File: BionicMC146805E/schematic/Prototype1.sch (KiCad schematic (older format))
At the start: 10 parts, among them SW1 TSD1265, U1 MC146805E2P, U2 74HCT541

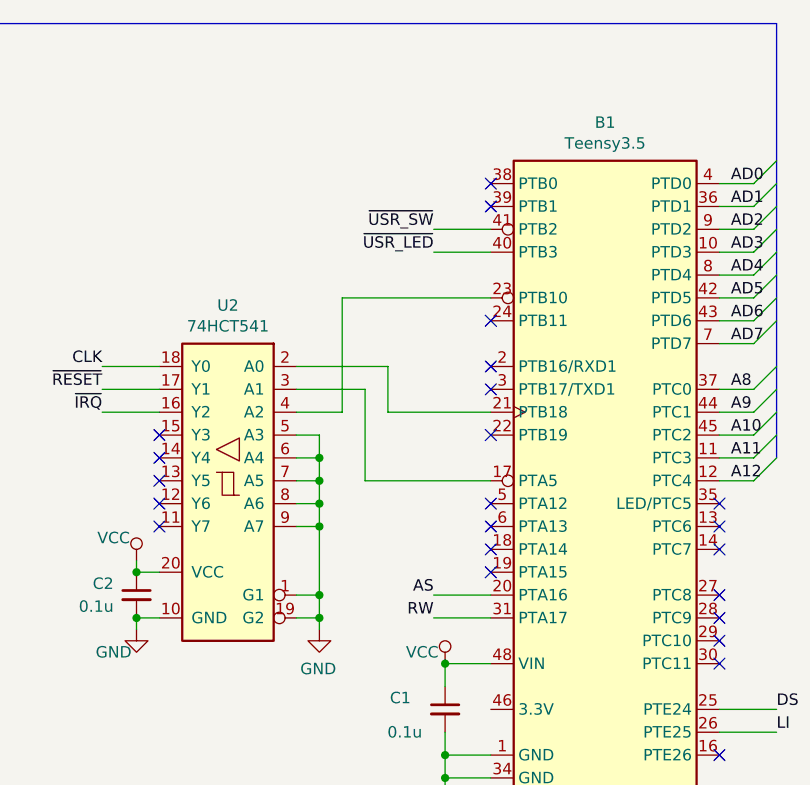
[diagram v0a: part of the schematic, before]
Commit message: [BionicMC146805E] Update to BionicBase/Teensy35 configuration
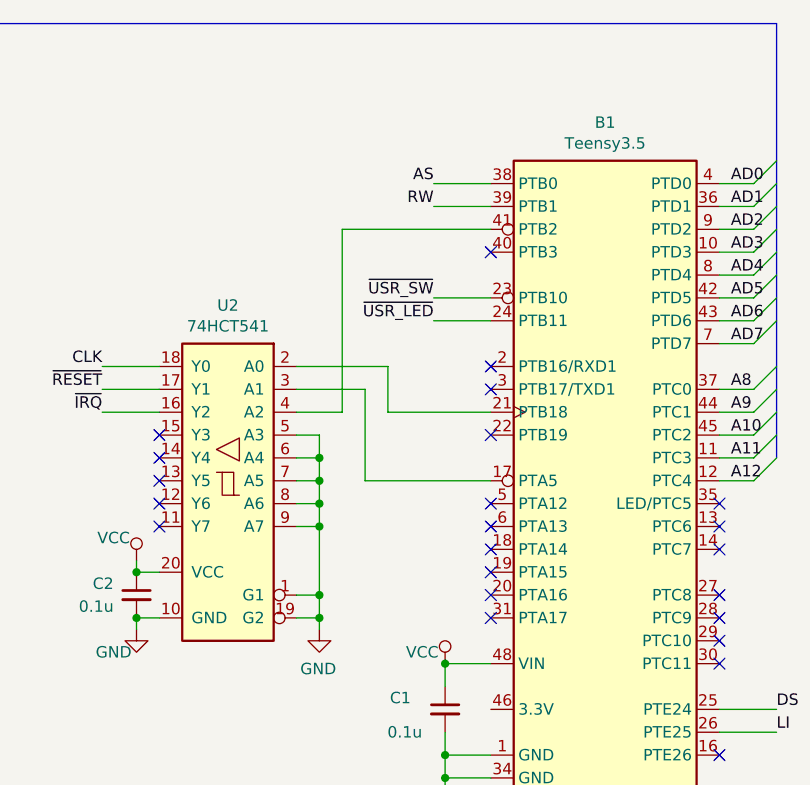
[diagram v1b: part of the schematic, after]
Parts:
- U2: footprint (none) -> Package_DIP:DIP-20_W7.62mm
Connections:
- net AS: now also B1.38 (PTB0); no longer B1.20 (PTA16)
- net RW: now also B1.39 (PTB1); no longer B1.31 (PTA17)
- net ~USR_LED~: now also B1.24 (PTB11); no longer B1.40 (PTB3)
- net ~USR_SW~: now also B1.23 (PTB10); no longer B1.41 (PTB2)
- net at U2.4 (A2): now also B1.41 (PTB2); no longer B1.23 (PTB10)
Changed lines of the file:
@@
 Text Label 4150 2900 2    50   ~ 0
 CLK
-Text Label 5600 2300 2    50   ~ 0
+Text Label 5600 2600 2    50   ~ 0
 ~USR_SW~
-Text Label 5600 2400 2    50   ~ 0
+Text Label 5600 2700 2    50   ~ 0
 ~USR_LED~
 Wire Wire Line
@@
 Text Label 1850 3600 2    50   ~ 0
 AS
-Text Label 5600 3900 2    50   ~ 0
+Text Label 5600 2100 2    50   ~ 0
 AS
-Text Label 5600 4000 2    50   ~ 0
+Text Label 5600 2200 2    50   ~ 0
 RW
 Wire Wire Line
@@
 F 0 "U2" H 4700 4167 50  0000 C CNN
 F 1 "74HCT541" H 4700 4076 50  0000 C CNN
-F 2 "" H 4700 3400 50  0001 C CNN
+F 2 "Package_DIP:DIP-20_W7.62mm" H 4700 3400 50  0001 C CNN
 F 3 "" H 4700 3400 50  0001 C CNN
 	1    4700 3400
@@
 	4150 2900 4400 2900
 Wire Wire Line
-	5600 3900 5850 3900
-Wire Wire Line
-	5600 4000 5850 4000
+	5600 2100 5850 2100
+Wire Wire Line
+	5600 2200 5850 2200
 Wire Wire Line
 	2150 3200 1850 3200
@@
 NoConn ~ 2150 2600
 NoConn ~ 2150 4000
-NoConn ~ 5850 2100
-NoConn ~ 5850 2200
 Wire Bus Line
 	7100 1400 3300 1400
@@
 NoConn ~ 4400 3600
 Wire Wire Line
-	5600 2300 5850 2300
-Wire Wire Line
-	5600 2400 5850 2400
+	5600 2600 5850 2600
+Wire Wire Line
+	5600 2700 5850 2700
 Text Label 1850 3100 2    50   ~ 0
 ~RESET~
@@
 Text Label 7100 4500 0    50   ~ 0
 LI
-NoConn ~ 5850 2700
 Wire Wire Line
 	4150 3100 4400 3100
 Wire Wire Line
 	5000 3100 5200 3100
-Wire Wire Line
-	5200 3100 5200 2600
-Wire Wire Line
-	5200 2600 5850 2600
 NoConn ~ 5850 3500
 NoConn ~ 5850 3600
@@
 	1    0    0    -1
 $EndComp
+Wire Wire Line
+	5850 2300 5200 2300
+Wire Wire Line
+	5200 2300 5200 3100
+NoConn ~ 5850 3900
+NoConn ~ 5850 4000
+NoConn ~ 5850 2400
 Wire Bus Line
 	3300 1400 3300 3200

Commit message: [BionicMC146805E] Mezzanine board
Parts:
- removed B1: Teensy3.5, Package_DIP:DIP-48_W15.24mm, symbol 0-LocalLibrary:Teensy3.5
- removed C1, C2: 0.1u, Capacitor_THT:C_Disc_D3.4mm_W2.1mm_P2.50mm, symbol Device:C_Small
- removed C4: 22p, symbol Device:C_Small
- removed R1: 33, symbol Device:R_Small
- removed R6: 560, Resistor_THT:R_Axial_DIN0204_L3.6mm_D1.6mm_P5.08mm_Horizontal, symbol Device:R_Small
- removed SW1: TSD1265, 0-LocalLibrary:SW_PUSH-LED-12mm, symbol 0-LocalLibrary:SW_Push_LED
- removed U2: 74HCT541, Package_DIP:DIP-20_W7.62mm, symbol 0-LocalLibrary:74HC541
- added J1: BionicConnector, 0-LocalLibrary:DIP-48_W10.16mm, symbol 0-LocalLibrary:BionicConnector
- renumbered C3 to C2
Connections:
- net GND: now also J1.48 (GND)
- net VCC: now also J1.25 (VCC)
- net P46: now reaches U1.39 (OSC1)
- net P46: now also J1.32 (P46)
- net P44: now reaches U1.31 (PB5)
- net P44: now also J1.34 (P44)
- net P45: now reaches U1.32 (PB4)
- net P45: now also J1.33 (P45)
- net P36: now reaches U1.33 (PB3)
- net P36: now also J1.40 (P27)
- net P35: now reaches U1.34 (PB2)
- net P35: now also J1.41 (P26)
- net P34: now reaches U1.35 (PB1)
- net P34: now also J1.42 (P25)
- net A10 renamed P22
- net P22: now also J1.13 (P32)
- net A11 renamed P23
- net P23: now also J1.14 (P33)
- net A12 renamed P24
- net P24: now also J1.15 (P34)
- net A8 renamed P20
- net P20: now also J1.11 (P30)
- net A9 renamed P21
- net P21: now also J1.12 (P31)
- net AD0 renamed P10
- net P10: now also J1.2 (P10)
- net AD1 renamed P11
- net P11: now also J1.3 (P11)
- net AD2 renamed P12
- net P12: now also J1.4 (P12)
- net AD3 renamed P13
- net P13: now also J1.5 (P13)
- net AD4 renamed P14
- net P14: now also J1.6 (P14)
- net AD5 renamed P15
- net P15: now also J1.7 (P15)
- net AD6 renamed P16
- net P16: now also J1.8 (P16)
- net AD7 renamed P17
- net P17: now also J1.9 (P17)
- net AS renamed P41
- net P41: now also J1.37 (P41)
- net DS renamed P50
- net LI renamed P51
- net RW renamed P40
- net P40: now also J1.38 (P40)
- net ~IRQ~ renamed P42
- net P42: now also J1.36 (P42)
- net ~RESET~ renamed P53
- net P53: now also J1.23 (P53)
- new net P43: J1.35 (P43)
- new net P47: J1.31 (P47)
- no-connect marks 41 -> 29
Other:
- moved on the sheet: C2

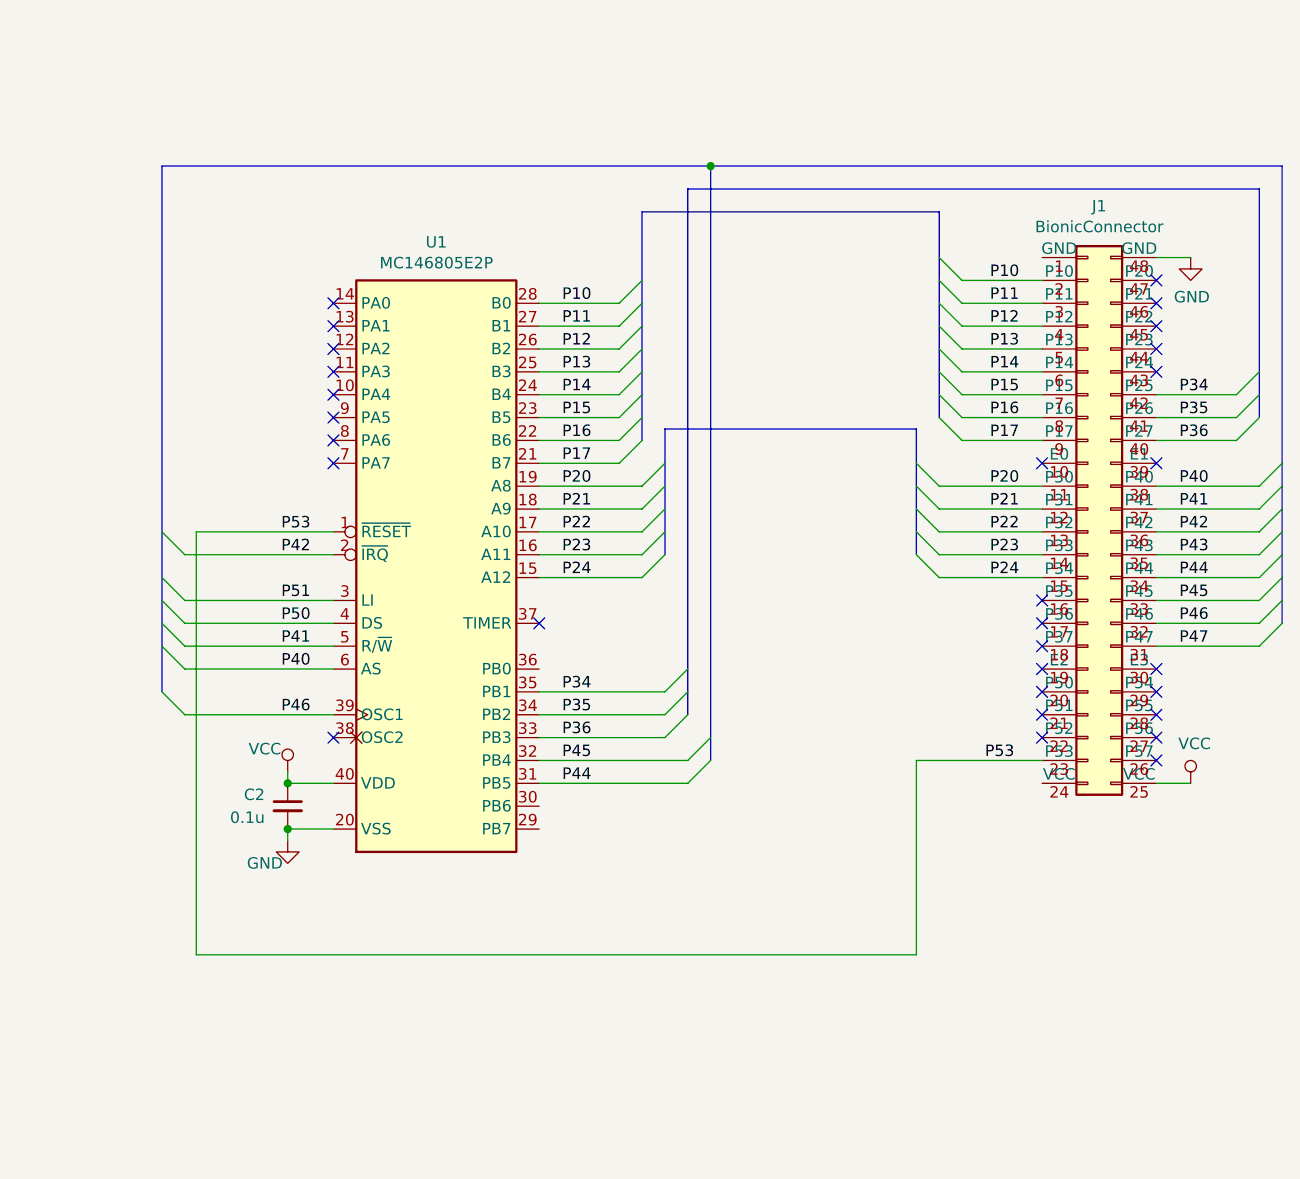
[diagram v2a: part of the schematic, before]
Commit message: [BionicMC146805E] Tune bus cycle
- Teensy 4.1: OSC1 ~ 4MHz, AS/DS ~ 800kHz
- Teensy 3.5: OSC1 ~ 1MHz, AS/DS ~ 200kHz
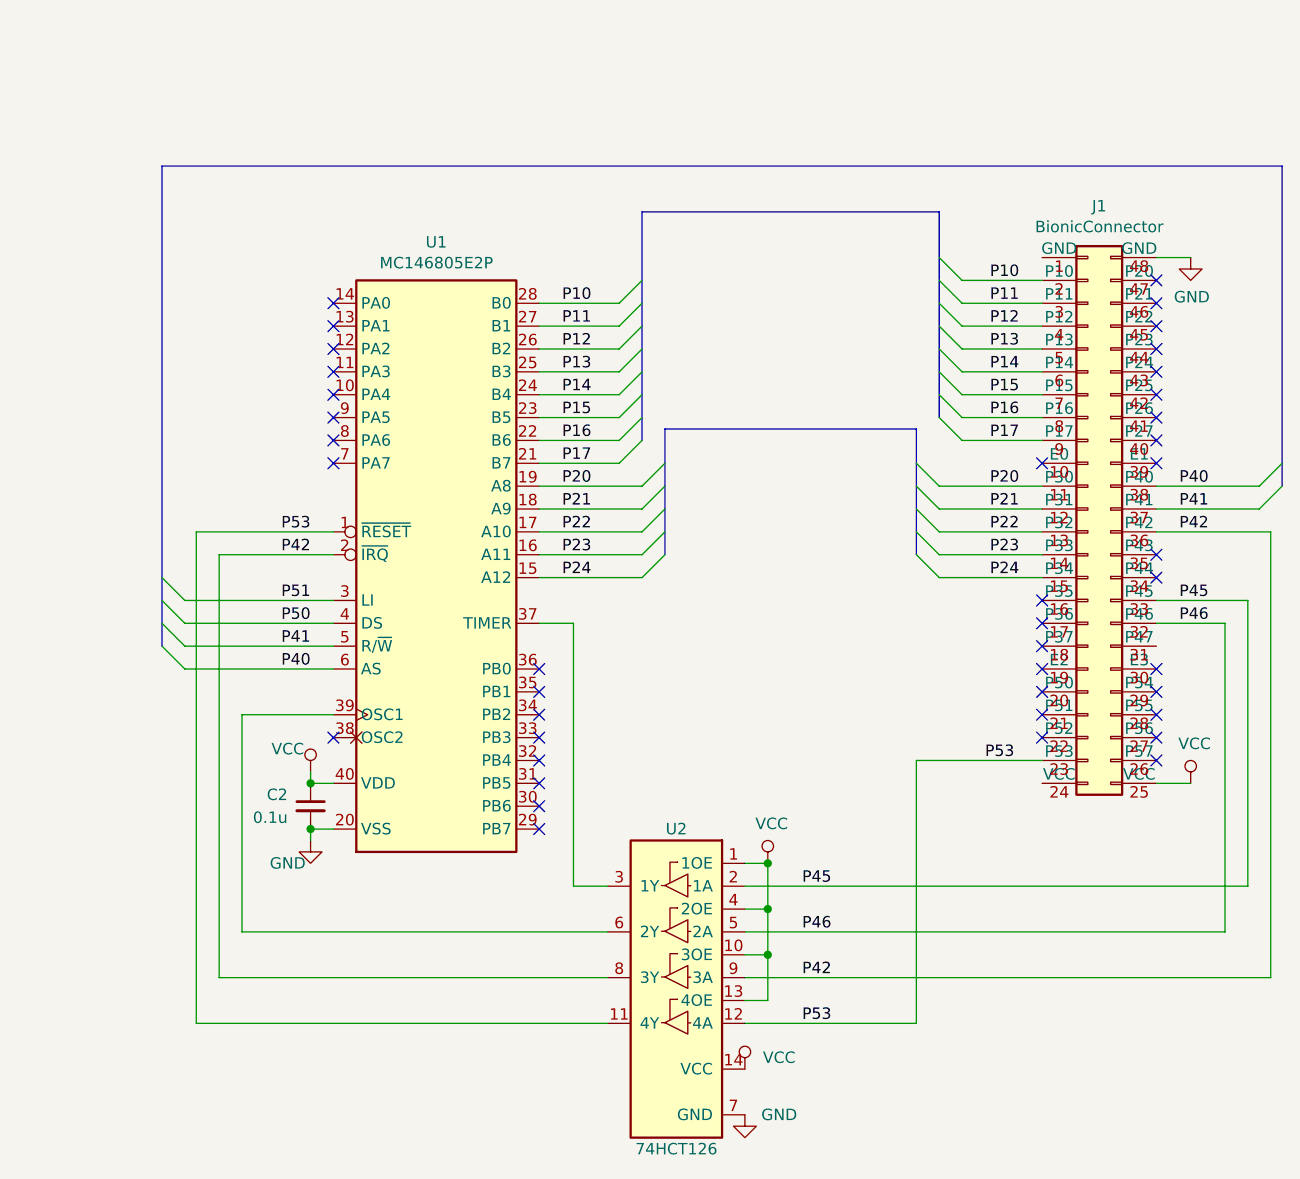
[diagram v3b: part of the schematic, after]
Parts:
- added U2: 74HCT126, Package_DIP:DIP-14_W7.62mm, symbol 0-LocalLibrary:74HCT126
- J1: footprint 0-LocalLibrary:DIP-48_W10.16mm -> 0-LocalLibrary:DIP-48_W7.62mm
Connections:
- net GND: now also U2.7 (GND)
- net P42: now also U2.8 (3Y), U2.9 (3A)
- net P45: now also U2.2 (1A); no longer U1.32 (PB4)
- net P46: now also U2.5 (2A); no longer U1.39 (OSC1)
- net P53: now also U2.11 (4Y), U2.12 (4A)
- net VCC: now also U2.1 (1OE), U2.10 (3OE), U2.13 (4OE), U2.14 (VCC), U2.4 (2OE)
- net at U1.37 (TIMER): now also U2.3 (1Y)
- net P34: no longer names the net of J1.42 (P25)
- net P34: no longer U1.35 (PB1)
- net P35: no longer names the net of J1.41 (P26)
- net P35: no longer U1.34 (PB2)
- net P36: no longer names the net of J1.40 (P27)
- net P36: no longer U1.33 (PB3)
- net P43: no longer names the net of J1.35 (P43)
- net P44: no longer names the net of J1.34 (P44)
- net P44: no longer U1.31 (PB5)
- net P47: no longer names the net of J1.31 (P47)
- new net: U1.39 (OSC1), U2.6 (2Y)
- no-connect marks 29 -> 41
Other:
- moved on the sheet: C2

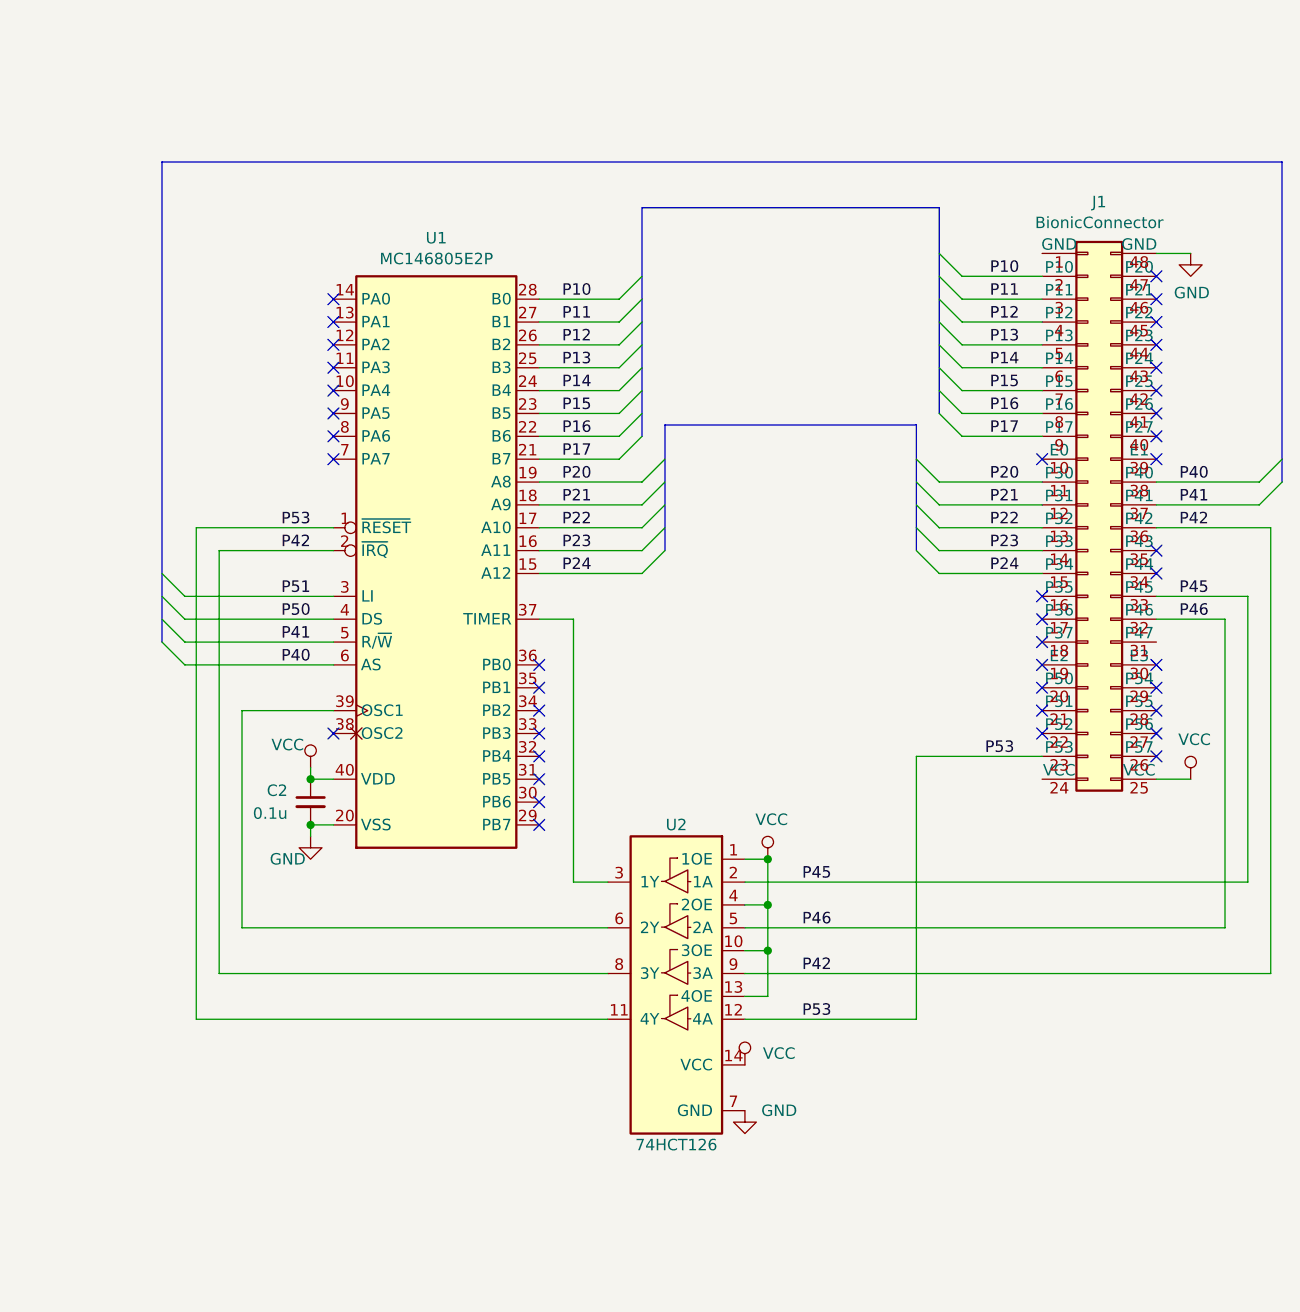
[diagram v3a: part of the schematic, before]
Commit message: Fix Bionic connector pin outs
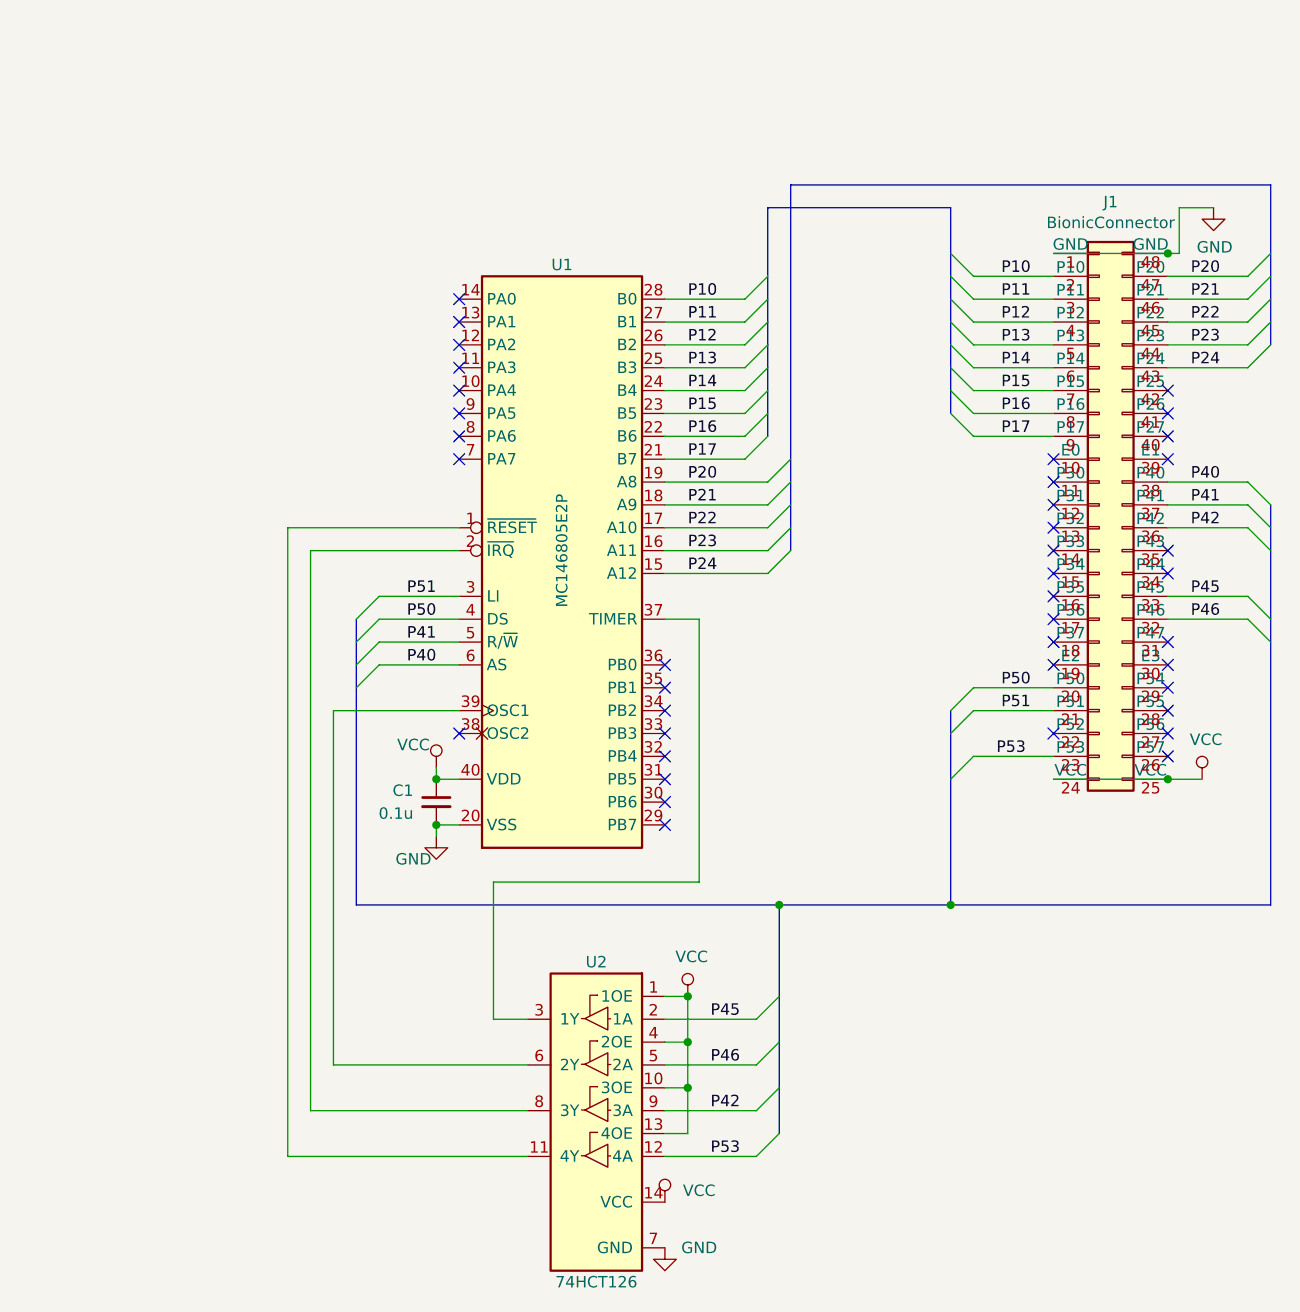
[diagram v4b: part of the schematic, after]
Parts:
- renumbered C2 to C1
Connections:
- net GND: now also J1.1 (GND)
- net P20: now also J1.47 (P20); no longer J1.11 (P30)
- net P21: now also J1.46 (P21); no longer J1.12 (P31)
- net P22: now also J1.45 (P22); no longer J1.13 (P32)
- net P23: now also J1.44 (P23); no longer J1.14 (P33)
- net P24: now also J1.43 (P24); no longer J1.15 (P34)
- net P42: no longer U1.2 (~IRQ~), U2.8 (3Y)
- net P50: now also J1.20 (P50)
- net P51: now also J1.21 (P51)
- net P53: no longer U1.1 (~RESET~), U2.11 (4Y)
- net VCC: now also J1.24 (VCC)
- new net: U1.1 (~RESET~), U2.11 (4Y)
- new net: U1.2 (~IRQ~), U2.8 (3Y)
- no-connect marks 41 -> 40
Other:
- moved on the sheet: C1, U2
